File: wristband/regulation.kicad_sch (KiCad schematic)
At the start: 3 parts, among them U5 MCP1700T-3302E/TT

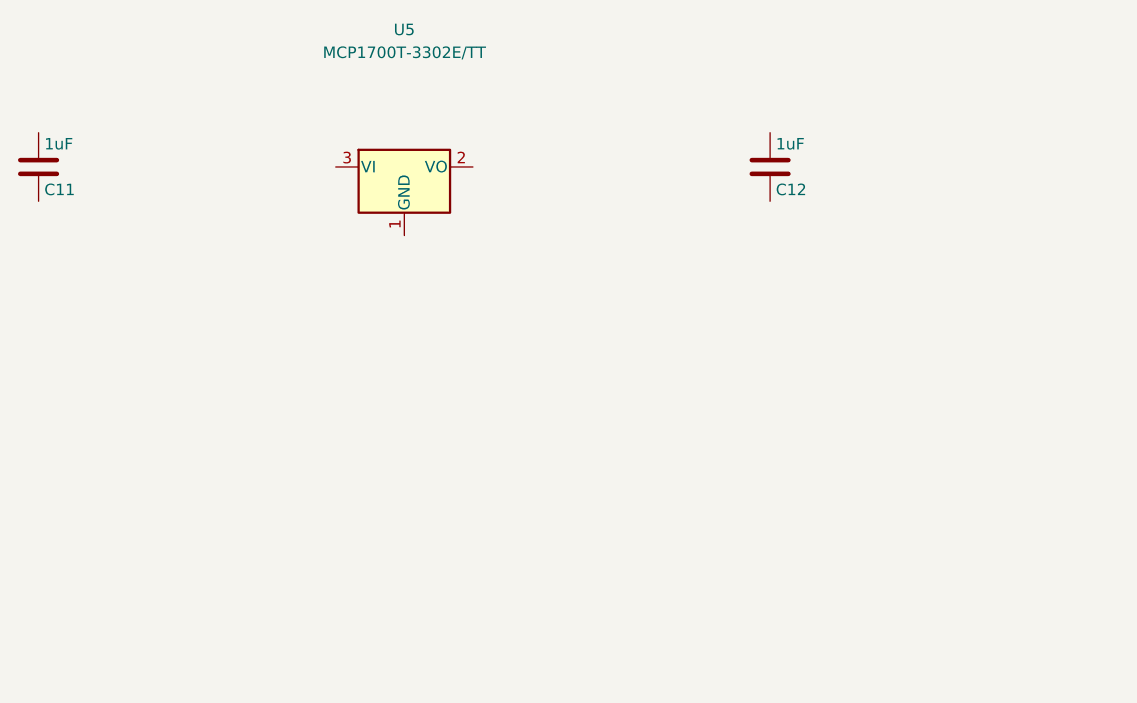
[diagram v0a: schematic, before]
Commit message: Land the wristband branch on main: DWM3001C wiring, TPS7A02 LDO, PCB (#5)
Brings six months of `dwm3001c-migration` onto current `main` as one commit.
A true rebase was attempted first and abandoned: the branch's own first
commit is a NINA-B400 migration that commit five then throws away, so
replaying it meant resolving 16 files of conflict for a design state nobody
wants. Squashed to a single three-way merge instead -- 18 conflicts, one
pass.

Both sides had independently migrated the wristband to the DWM3001C, so this
was not a fast-forward. Resolution, by ERC evidence rather than recency:

  main's wristband     104 violations, 93 errors
  branch's wristband     1 violation,   0 errors

main's 93 are 80 pin_not_connected + 10 power_pin_not_driven + 3
pin_not_driven -- PR #1 swapped in a fresh radio sheet and never wired it.
The branch wired it. So the branch's schematics are the base here, not
main's.

Taken from the branch: radio_mcu, regulation, programming_debug,
power_bms, mechanical, libs/, the PCB (9.8k lines, main has none), and the
DWM3001C footprint placeholder.

Taken from main: all project-wide docs. The branch's were stale on the bay
station -- still ESP32-S3 and DWM3000, which main replaced with BT840 and
DW3210.

Reconciled by hand:
- wristband.kicad_sch now carries main's 7-sheet hierarchy. `antenna` is
  dropped (DWM3001C has both antennas on-module); `indicators` and
  `testpoints` are spliced in from main verbatim, UUIDs preserved, so their
  child sheets' instance paths still resolve -- both roots share the root
  UUID b3417696, and the paths check out.
- decisions.md, passives-reference.md and wristband/README.md carried main's
  MCP1700 as the wristband LDO. Rewritten for the TPS7A02, with the swap's
  rationale ported from the branch rather than restated.
- README sheet table corrected: main marked every sheet "Placement only",
  which is no longer true for the five the branch wired.
- Dropped NINA-B400-55_PLACEHOLDER.kicad_mod; that part is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
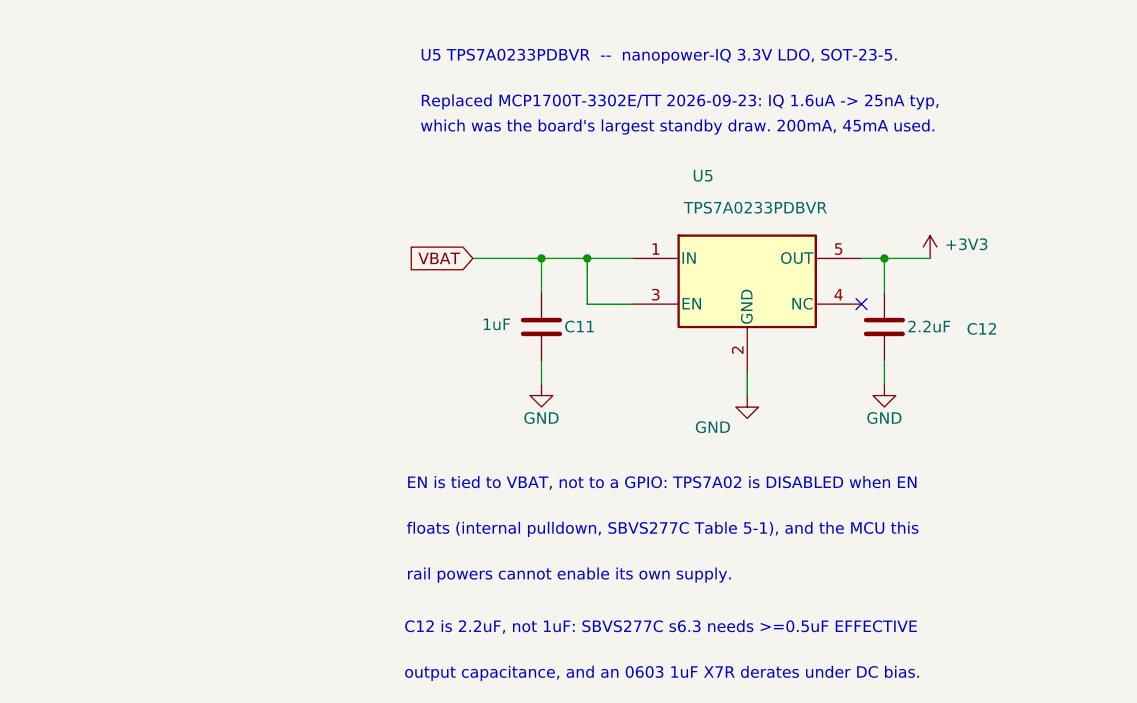
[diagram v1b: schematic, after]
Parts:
- removed U5: MCP1700T-3302E/TT, Package_TO_SOT_SMD:SOT-23, symbol Regulator_Linear:MCP1700x-330xxTT
- added U5: TPS7A0233PDBVR, Package_TO_SOT_SMD:SOT-23-5, symbol wristband:TPS7A0233PDBVR
- C11: MPN (none) -> CL10B105KA8NNNC; Manufacturer (none) -> Samsung Electro-Mechanics
- C12: value 1uF -> 2.2uF; MPN (none) -> CL10B105KA8NNNC; Manufacturer (none) -> Samsung Electro-Mechanics
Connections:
- net +3V3: now reaches C12.1
- net +3V3: now also U5.5 (OUT)
- net GND: now reaches C12.2
- net GND: now also C11.2, U5.2 (GND)
- net VBAT: now reaches C11.1
- net VBAT: now also U5.1 (IN), U5.3 (EN)
- no-connect marks 0 -> 1
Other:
- note added: "C12 is 2.2uF, not 1uF: SBVS277C s6.3 needs >=0.5uF EFFECTIVE"
- note added: "EN is tied to VBAT, not to a GPIO: TPS7A02 is DISABLED when EN"
- note added: "Replaced MCP1700T-3302E/TT 2026-09-23: IQ 1.6uA -> 25nA typ,"
- note added: "U5 TPS7A0233PDBVR -- nanopower-IQ 3.3V LDO, SOT-23-5."
- note added: "floats (internal pulldown, SBVS277C Table 5-1), and the MCU this"
- note added: "output capacitance, and an 0603 1uF X7R derates under DC bias."
- note added: "rail powers cannot enable its own supply."
- note added: "which was the board's largest standby draw. 200mA, 45mA used."
- moved on the sheet: C11, C12
